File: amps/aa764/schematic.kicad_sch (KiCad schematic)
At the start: 36 parts, among them T1 125P1B, T2 125A35A

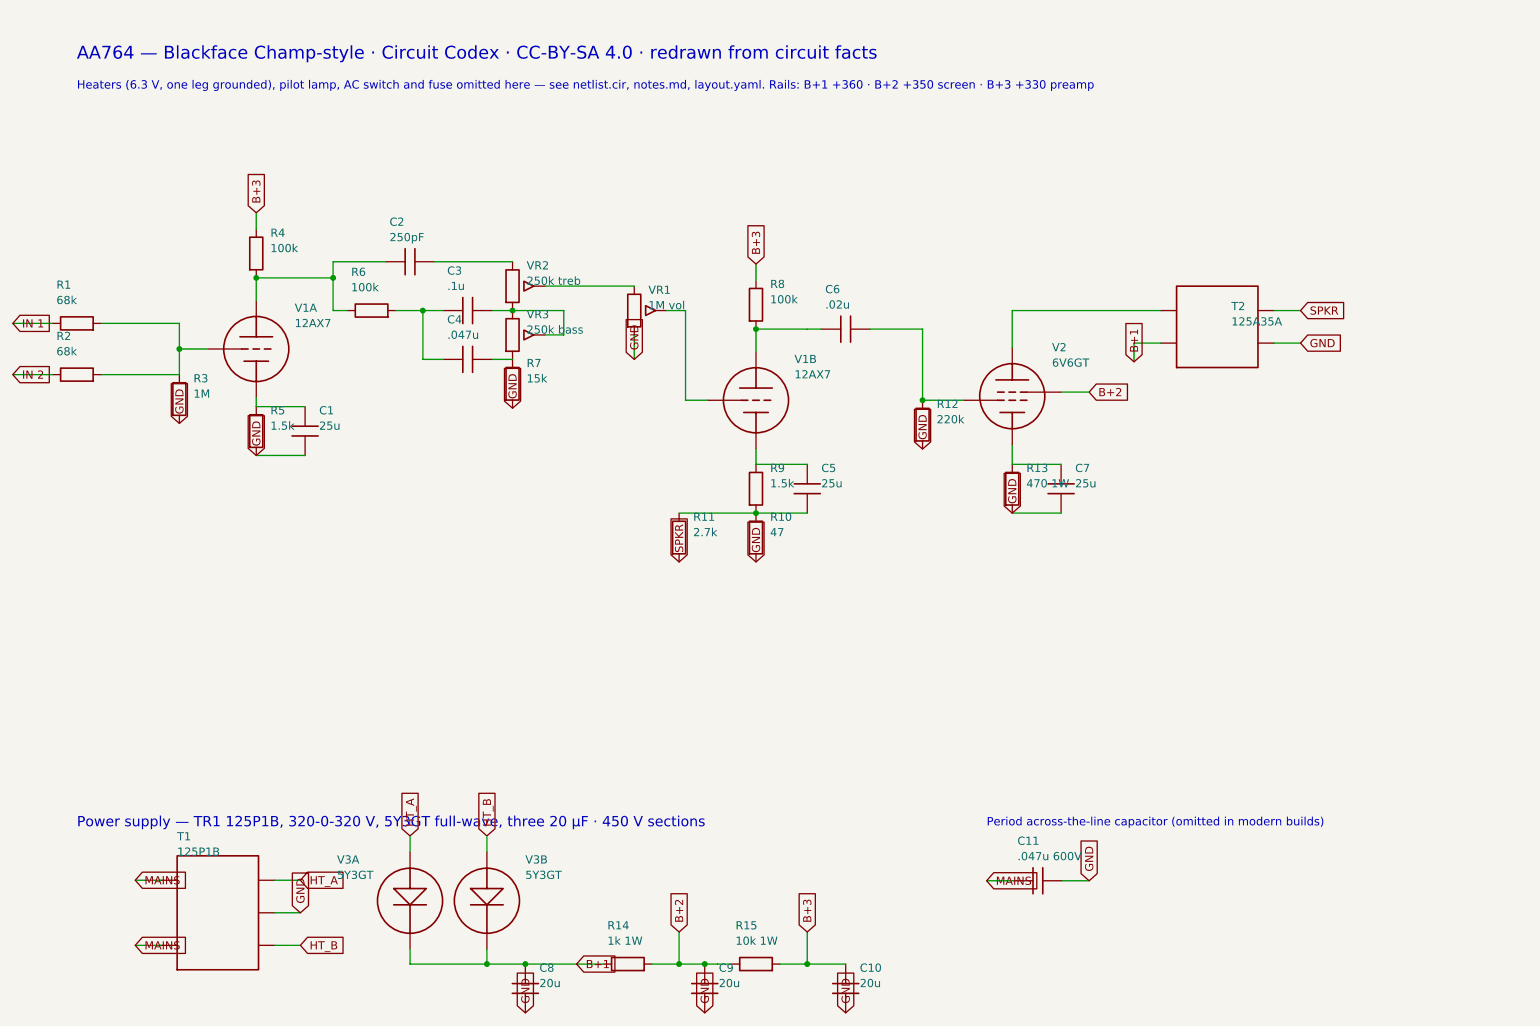
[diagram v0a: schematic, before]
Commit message: Fix: schematic sheets — real title block, fitted paper, no lettering through circuitry
Every sheet in the corpus shipped with an EMPTY title block ("Title:" and
"Date:" blank, default "Sheet /" furniture) laid onto a fixed A4/A3 page
regardless of the drawing's size, with prose annotations placed by hand
wherever a coordinate looked free when the amp was first drawn. The result
read as an unfinished alpha under a `verified` badge: KiCanvas's default view
is `zoom_to_page()`, so a 150 x 110 mm circuit on an A3 sheet opened as a
postage stamp, and later edits had pushed live circuitry under the prose.

schematic_lib.py — the builder now records each element as a (kind, points,
extra) tuple instead of a finished string, so `write()` can measure and move
what it emits:

- emits a real `(title_block …)` read from the amp's own meta.yaml — Title =
  designation + style, Date = the verification (or added) date, Rev = the
  verification status, Company = Circuit Codex, plus the licence and source
  URL as comments. Fixes all 34 sheets from one place;
- emits `(paper "User" w h)` cut to the drawing, translated to a fixed margin,
  with the bottom 34 mm strip reserved for the worksheet's title block. Sheet
  utilisation of the drawable area went from as low as ~20% to 92-98%;
- `note()` queues prose into a wrapped band under the circuit, and `caption()`
  places a section heading over the block it names, nudging it clear if it
  would print through anything;
- per-symbol default label offsets (the old single default printed every pot's
  value through its own wiper arrow and every transformer's designator through
  its body), plus `place_labels()`, which moves any designator/value block that
  would print over ink;
- transformers and chokes are drawn, not boxed: iron core between two windings,
  centre taps where the part has them, and an optional `spec` lettering slot for
  a ratio or impedance;
- `gnd()` takes a direction, because a flag defaulting to "down" at the HEAD of
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
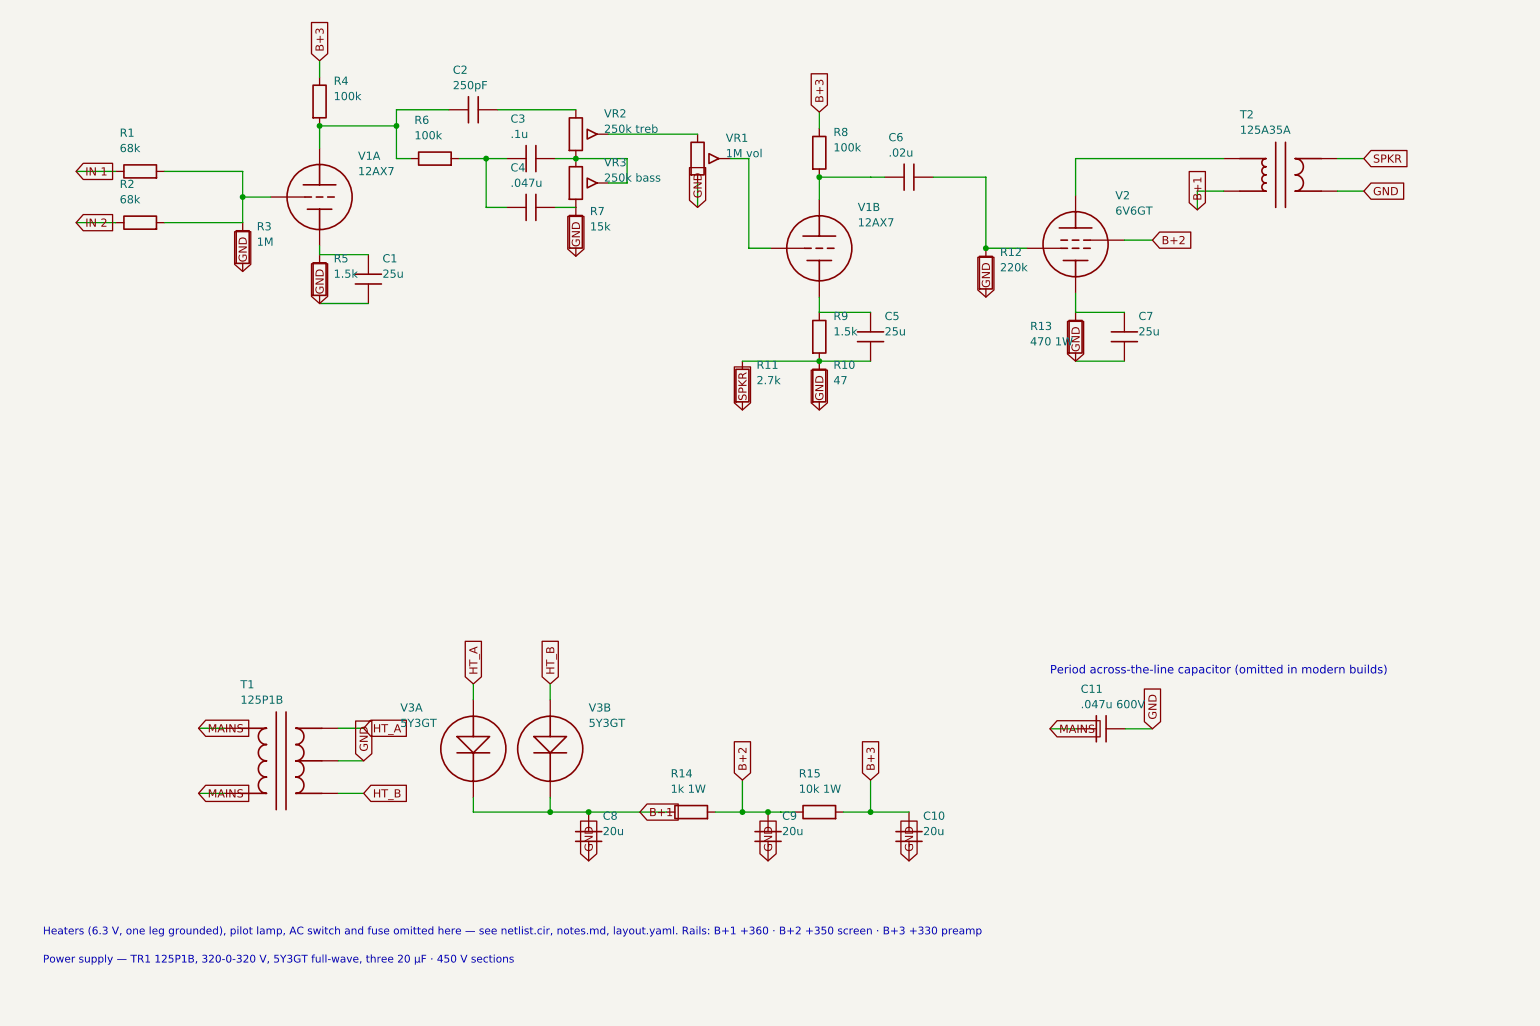
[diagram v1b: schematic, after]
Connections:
- net at C3.2, VR2.3, VR3.1: no longer VR3.2 (W)
- net at VR2.2 (W): no longer VR1.1
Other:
- note removed: "AA764 — Blackface Champ-style · Circuit Codex · CC-BY-SA 4.0 · redrawn from circuit facts"
- company: (none) -> Circuit Codex
- title: (none) -> AA764 — Blackface Champ-style
